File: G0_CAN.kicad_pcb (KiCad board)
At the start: 2 copper layers, 69.8 x 53.3 mm, 31 parts, among them J1 USB_C_Receptacle_USB2.0, J2 CAN1, J3 CAN2, U1 Nucleo-64-G0B1, U2 TJA1051TK-3, U3 TJA1051TK-3

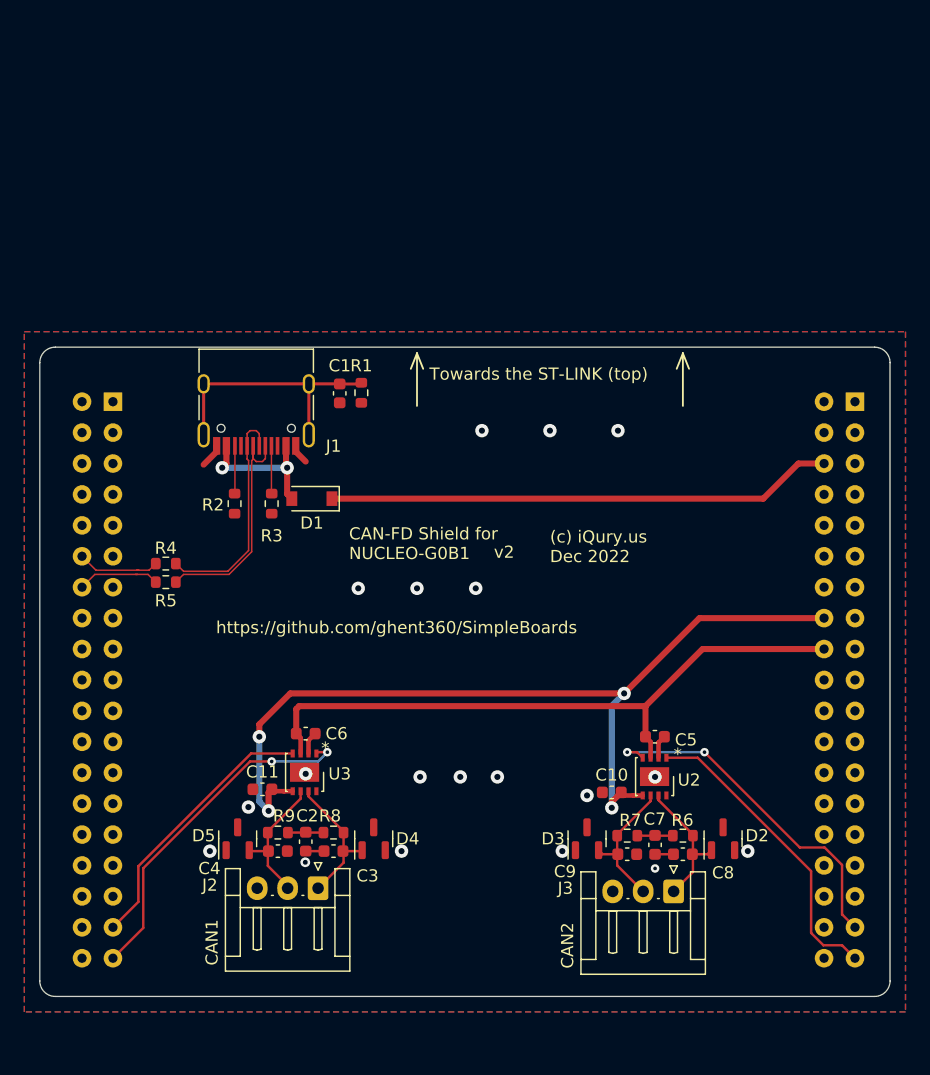
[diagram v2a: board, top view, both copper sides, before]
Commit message: Make the G0-CAN board use isolated CAN.
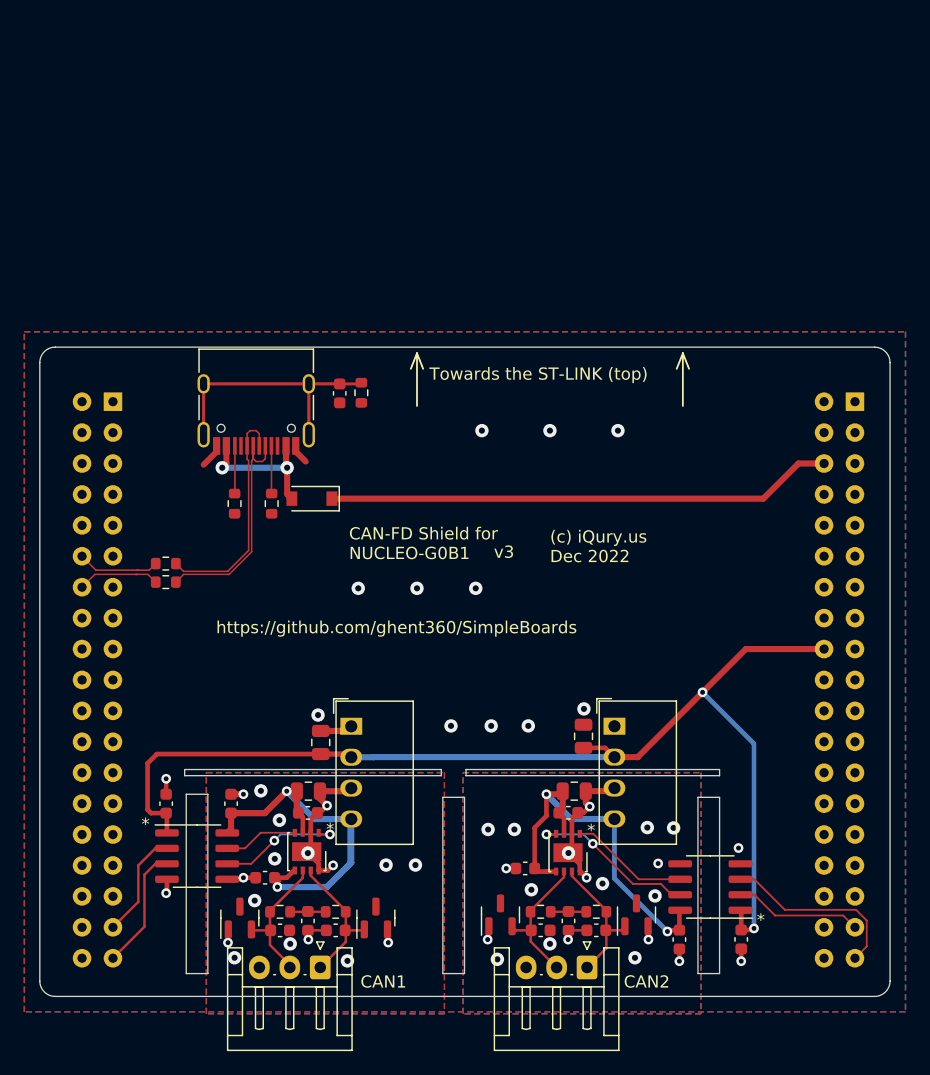
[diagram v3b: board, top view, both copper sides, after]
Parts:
- added C12: 4.7uF, Capacitor_SMD:C_0805_2012Metric, F.Cu at (96.0, 100.0)
- added C13: 4.7uF, Capacitor_SMD:C_0805_2012Metric, F.Cu at (96.7, 95.5)
- added C14: 4.7uF, Capacitor_SMD:C_0805_2012Metric, F.Cu at (74.1, 100.0)
- added C15: 4.7uF, Capacitor_SMD:C_0805_2012Metric, F.Cu at (75.1, 96.0)
- added C16: 100nF, Capacitor_SMD:C_0603_1608Metric, F.Cu at (62.4, 101.0)
- added C17: 100nF, Capacitor_SMD:C_0603_1608Metric, F.Cu at (67.8, 101.0)
- added C18: 100nF, Capacitor_SMD:C_0603_1608Metric, F.Cu at (109.7, 112.2)
- added C19: 100nF, Capacitor_SMD:C_0603_1608Metric, F.Cu at (104.6, 112.2)
- added U4: CRE1S0505S3C, Converter_DCDC:Converter_DCDC_Murata_CRE1xxxxxx3C_THT, F.Cu at (99.3, 94.6)
- added U5: CRE1S0505S3C, Converter_DCDC:Converter_DCDC_Murata_CRE1xxxxxx3C_THT, F.Cu at (77.7, 94.6)
- added U6: ADuM1201BR, Package_SO:SOIC-8_3.9x4.9mm_P1.27mm, F.Cu at (65.0, 105.3)
- added U7: ADuM1201BR, Package_SO:SOIC-8_3.9x4.9mm_P1.27mm, F.Cu at (107.2, 107.8)
- moved C10 9.47 mm to (91.9, 106.3)
- moved D3 9.47 mm to (89.9, 110.1)
- moved U2 9.47 mm to (95.5, 105.0)
- moved C5 9.47 mm to (95.5, 101.8)
- moved C7 9.47 mm to (95.5, 110.6)
- moved C8 9.47 mm to (97.8, 111.4)
- moved C9 9.47 mm to (93.2, 111.4)
- moved D2 9.47 mm to (101.1, 110.1)
- moved J3 9.47 mm to (97.0, 114.5)
- moved R6 9.47 mm to (97.8, 109.9)
- moved R7 9.47 mm to (93.2, 109.9)
- moved C11 7.27 mm to (70.6, 107.1)
- moved C3 6.51 mm to (76.4, 111.4)
- moved C4 6.51 mm to (71.8, 111.4)
- moved C6 6.51 mm to (74.1, 101.8)
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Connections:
- C10 pad 1: GND -> GND2
- C10 pad 2: /3.3V -> /5V-CAN2
- C11 pad 1: GND -> GND1
- C11 pad 2: /3.3V -> /5V-CAN1
- C2 pad 2: GND -> GND1
- C3 pad 2: GND -> GND1
- C4 pad 1: GND -> GND1
- C5 pad 1: /5V -> /5V-CAN2
- C5 pad 2: GND -> GND2
- C6 pad 1: /5V -> /5V-CAN1
- C6 pad 2: GND -> GND1
- C7 pad 2: GND -> GND2
- C8 pad 2: GND -> GND2
- C9 pad 1: GND -> GND2
- D2 pad 2: GND -> GND2
- D3 pad 1: GND -> GND2
- D4 pad 2: GND -> GND1
- D5 pad 1: GND -> GND1
- J2 pad 3: GND -> GND1
- J3 pad 3: GND -> GND2
- U2 pad 1: /CAN2_TX -> /CAN2_TX_ISO
- U2 pad 2: GND -> GND2
- U2 pad 3: /5V -> /5V-CAN2
- U2 pad 4: /CAN2_RX -> /CAN2_RX_ISO
- U2 pad 5: /3.3V -> /5V-CAN2
- U2 pad 8: GND -> GND2
- U2 pad 9: GND -> GND2
- U3 pad 1: /CAN1_TX -> /CAN1_TX_ISO
- U3 pad 2: GND -> GND1
- U3 pad 3: /5V -> /5V-CAN1
- U3 pad 4: /CAN1_RX -> /CAN1_RX_ISO
- U3 pad 5: /3.3V -> /5V-CAN1
- U3 pad 8: GND -> GND1
- U3 pad 9: GND -> GND1
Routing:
- net /3.3V: track 74.4 -> 0.00 mm, vias 4 -> 0
- net /5V: track 53.6 -> 96.2 mm, vias 0 -> 2
- net /5V-CAN1: track 0.00 -> 34.8 mm, vias 0 -> 2
- net /5V-CAN2: track 0.00 -> 33.8 mm, vias 0 -> 2
- net /CAN1_TX: track 28.4 -> 10.2 mm, vias 2 -> 0
- net /CAN2_RX: track 28.5 -> 10.5 mm, vias 2 -> 0
- net GND1: track 0.00 -> 17.0 mm, vias 0 -> 17
- net /CAN2_RX_ISO: track 0.00 -> 13.9 mm, vias 0 -> 2
- net GND2: track 0.00 -> 13.9 mm, vias 0 -> 19
- net /CAN1_RX: track 22.4 -> 8.88 mm
- net /CAN1_TX_ISO: track 0.00 -> 10.4 mm, vias 0 -> 2
- net /CAN2_TX: track 25.3 -> 15.3 mm
- net /CAN2_TX_ISO: track 0.00 -> 9.79 mm
- net /CAN1_RX_ISO: track 0.00 -> 6.09 mm
- net GND: track 10.4 -> 9.73 mm, vias 19 -> 15
- added copper zone on B.Cu, net GND1
- added copper zone on F.Cu, net GND1
- added copper zone on B.Cu, net GND2
- added copper zone on F.Cu, net GND2
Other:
- outline, holes or cut-outs redrawn
- board text added: "v3"
- board text removed: "v2"

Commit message: Flip the nucleo connector.
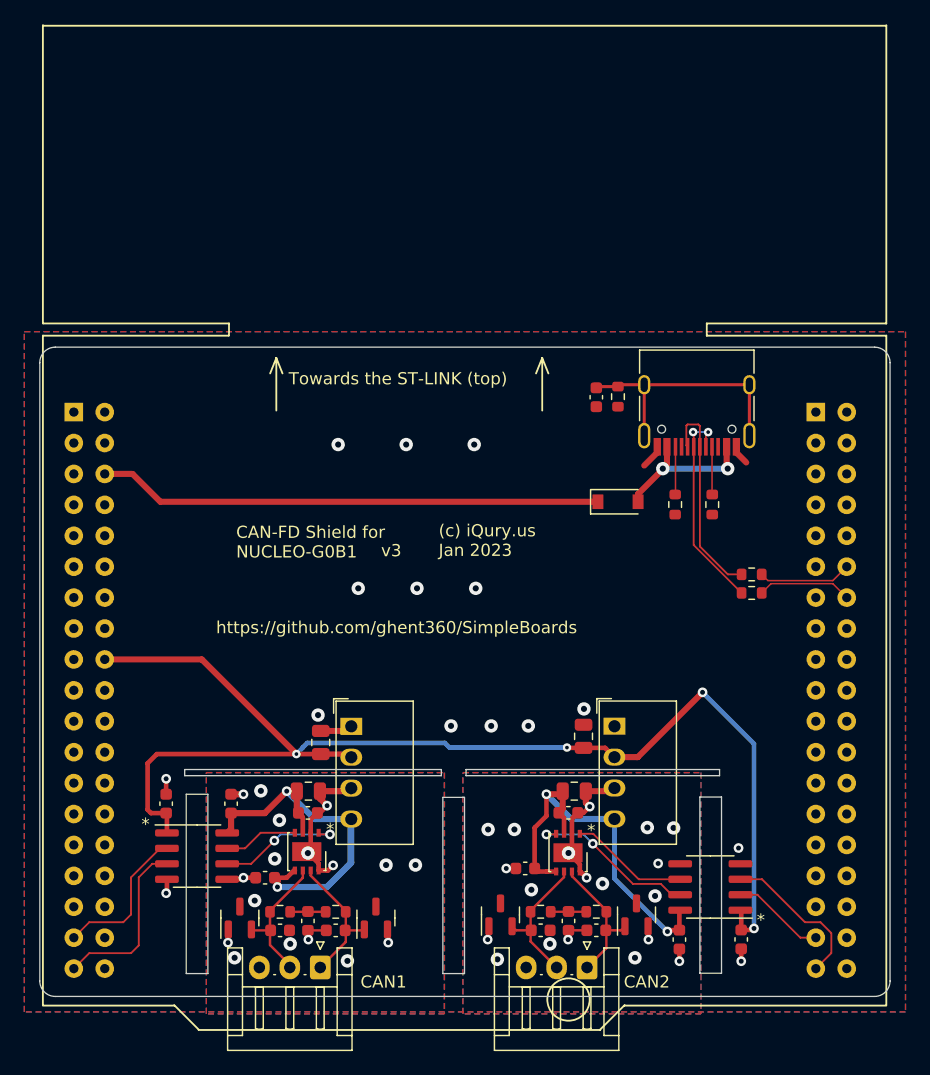
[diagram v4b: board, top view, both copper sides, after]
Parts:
- U1: moved to F.Cu
- U6, U7: value ADuM1201BR -> NSi8121N0
- moved U1 64.2 mm to (54.9, 114.6), turned to 0 degrees
- moved R4 48.1 mm to (110.6, 82.2), turned to 0 degrees
- moved R5 48.1 mm to (110.6, 83.7), turned to 0 degrees
- moved J1 36.2 mm to (106.0, 67.6)
- moved R2 36.2 mm to (104.3, 76.4)
- moved R3 36.2 mm to (107.3, 76.4)
- moved D1 25.1 mm to (99.6, 76.2), turned to 0 degrees
- moved C1 21.1 mm to (97.8, 67.6)
- moved R1 21.1 mm to (99.6, 67.6)
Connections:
- U1 pad 35: /CAN2_RX -> /CAN1_RX
- U1 pad 37: /CAN2_TX -> /CAN1_TX
- U1 pad 73: /CAN1_RX -> /CAN2_RX
- U1 pad 75: /CAN1_TX -> /CAN2_TX
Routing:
- net /5V: track 96.2 -> 106.3 mm, vias 2 -> 4
- net /CAN1_TX: track 10.2 -> 14.5 mm
- net /CAN1_RX: track 8.88 -> 12.5 mm
- net /CAN2_RX: track 10.5 -> 7.66 mm
- net /CAN2_TX: track 15.3 -> 12.7 mm
- net /D-: track 19.3 -> 17.4 mm, vias 0 -> 2
- net /D+: track 18.8 -> 17.3 mm
- net Net-(D1-A): track 11.8 -> 12.7 mm
- net /USB_DN: track 6.92 -> 7.78 mm
- net /USB_DP: track 6.92 -> 7.67 mm
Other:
- outline, holes or cut-outs redrawn
- board text added: "(c) iQury.us Jan 2023"
- board text removed: "(c) iQury.us Dec 2022"

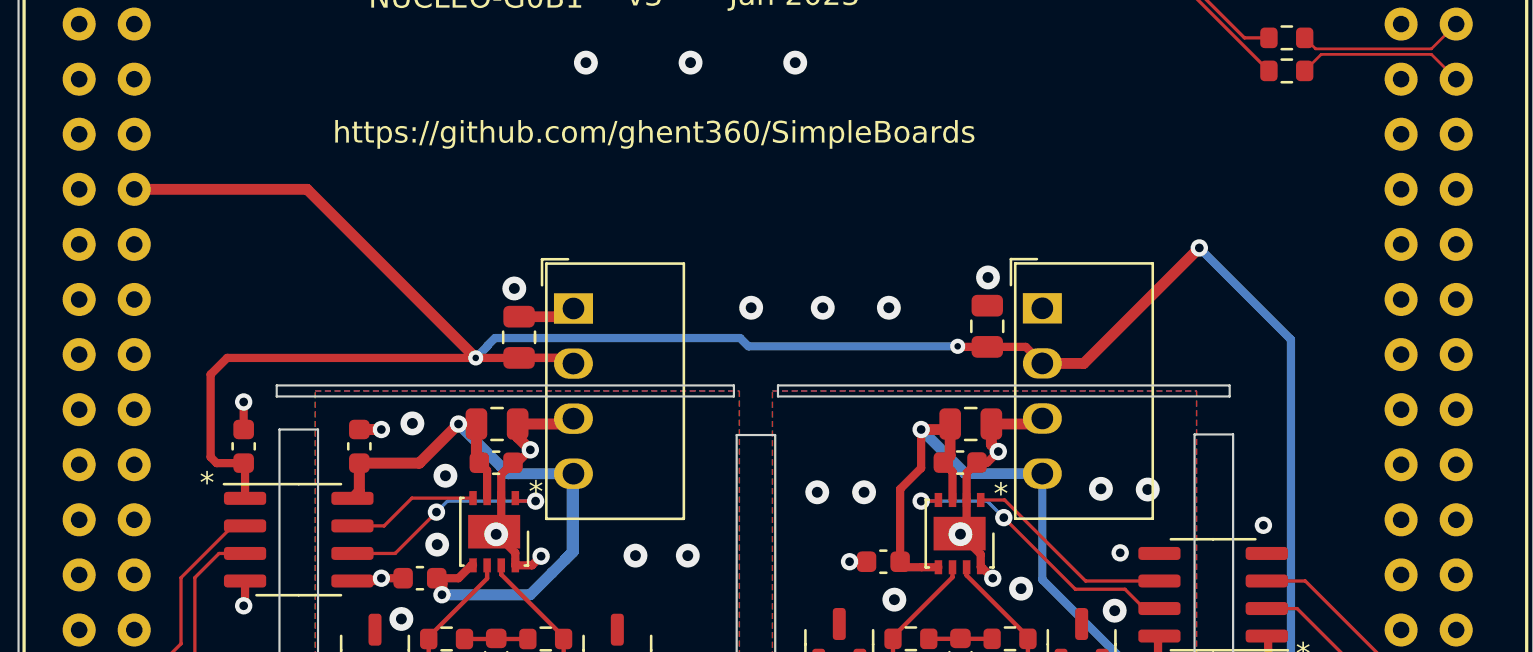
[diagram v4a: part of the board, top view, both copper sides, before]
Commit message: Add TX/RX leds to the CAN shield.
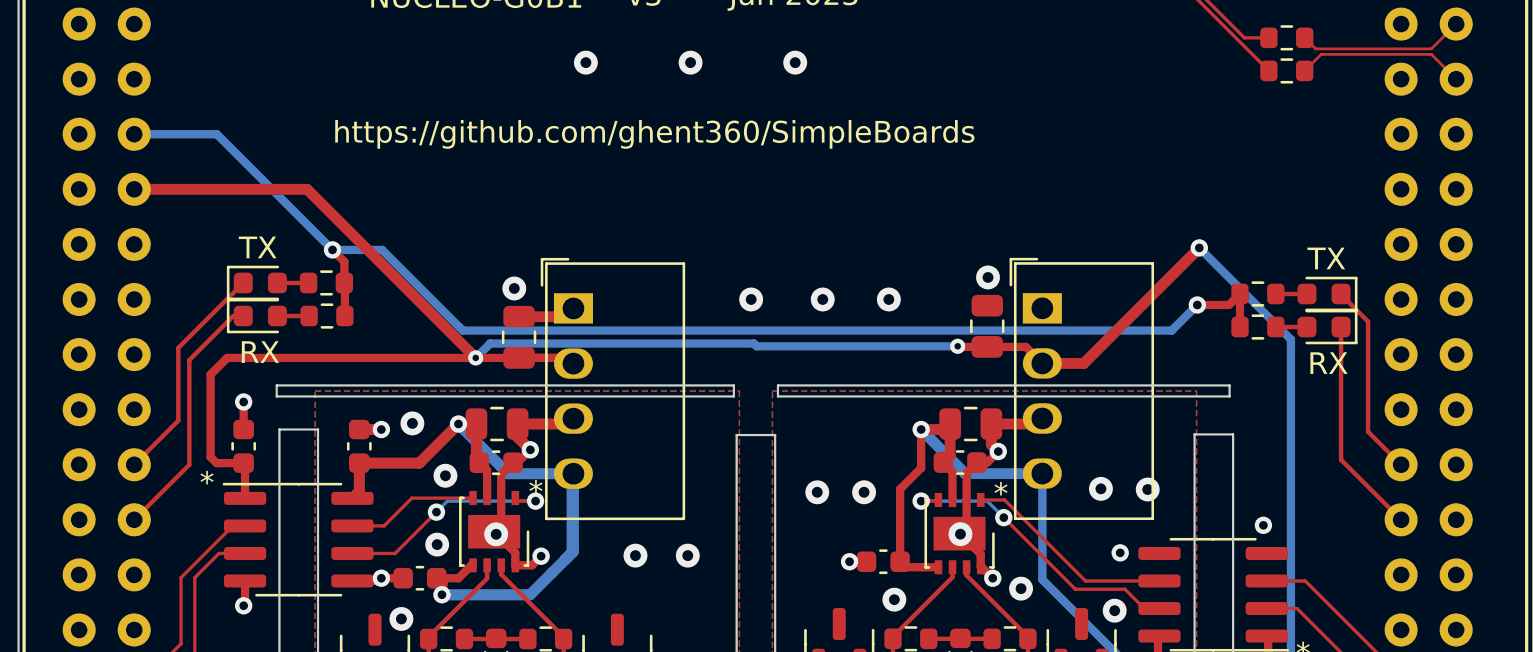
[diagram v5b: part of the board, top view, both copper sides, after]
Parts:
- added D6: TX, LED_SMD:LED_0603_1608Metric, F.Cu at (63.2, 93.5)
- added D7: TX, LED_SMD:LED_0603_1608Metric, F.Cu at (112.3, 94.0)
- added D8: RX, LED_SMD:LED_0603_1608Metric, F.Cu at (63.2, 95.0)
- added D9: RX, LED_SMD:LED_0603_1608Metric, F.Cu at (112.3, 95.5)
- added R10: 22, Resistor_SMD:R_0603_1608Metric, F.Cu at (66.3, 93.5)
- added R11: 22, Resistor_SMD:R_0603_1608Metric, F.Cu at (109.2, 94.0)
- added R12: 22, Resistor_SMD:R_0603_1608Metric, F.Cu at (66.3, 95.0)
- added R13: 22, Resistor_SMD:R_0603_1608Metric, F.Cu at (109.2, 95.5)
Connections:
- U1 pad 28: unconnected-(U1A-PA0) -> /CAN1_TX_LED
- U1 pad 30: unconnected-(U1A-PA1) -> /CAN1_RX_LED
- U1 pad 65: unconnected-(U1B-PB4) -> /CAN2_TX_LED
- U1 pad 67: unconnected-(U1B-PB5) -> /CAN2_RX_LED
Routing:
- net /3.3V: track 0.00 -> 60.2 mm, vias 0 -> 2
- net /CAN1_RX_LED: track 0.00 -> 11.7 mm
- net /CAN1_TX_LED: track 0.00 -> 10.5 mm
- net /CAN2_RX_LED: track 0.00 -> 10.0 mm
- net /CAN2_TX_LED: track 0.00 -> 9.02 mm
- net Net-(D8-A): track 0.00 -> 1.46 mm
- net Net-(D9-A): track 0.00 -> 1.44 mm
- net Net-(D7-A): track 0.00 -> 1.44 mm
- net Net-(D6-A): track 0.00 -> 1.44 mm
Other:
- board text added: "RX"
- board text added: "TX"

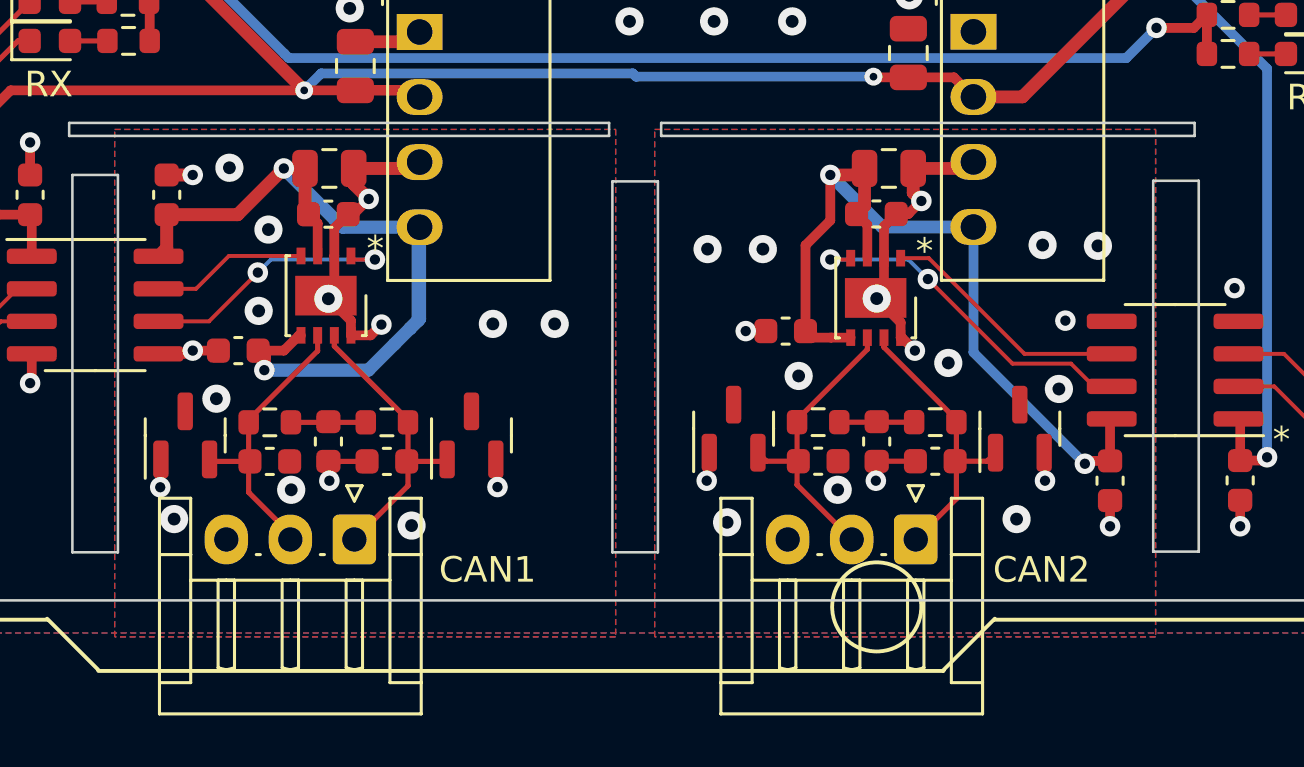
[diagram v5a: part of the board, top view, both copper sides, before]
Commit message: Add terminator jumpers.
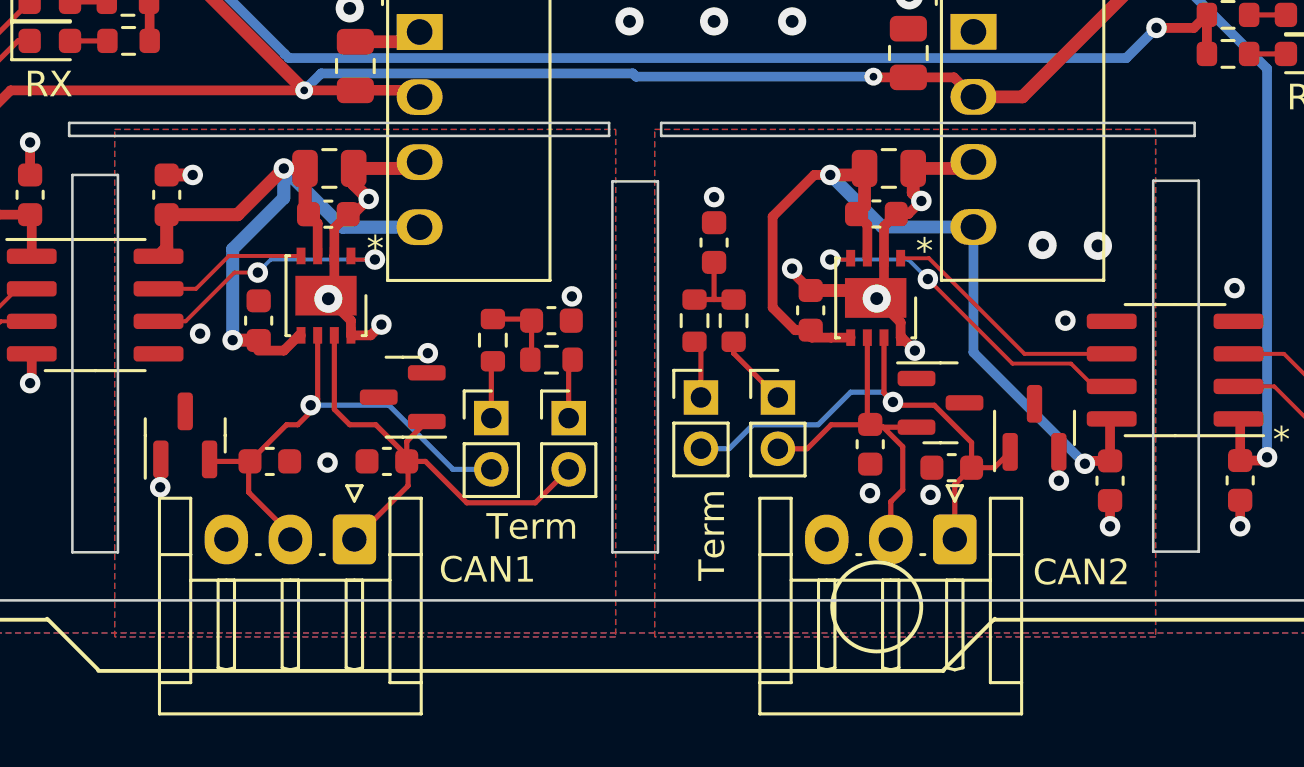
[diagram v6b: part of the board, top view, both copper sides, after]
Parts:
- added JP1: Trm, Connector_PinHeader_2.00mm:PinHeader_1x02_P2.00mm_Vertical, F.Cu at (88.6, 108.9)
- added JP2: Trm, Connector_PinHeader_2.00mm:PinHeader_1x02_P2.00mm_Vertical, F.Cu at (91.6, 108.9)
- added JP3: Trm, Connector_PinHeader_2.00mm:PinHeader_1x02_P2.00mm_Vertical, F.Cu at (83.5, 109.7)
- added JP4: Trm, Connector_PinHeader_2.00mm:PinHeader_1x02_P2.00mm_Vertical, F.Cu at (80.5, 109.7)
- moved R6 10.2 mm to (88.4, 105.9), turned to 90 degrees
- moved C7 10.0 mm to (89.2, 102.9), turned to 90 degrees
- moved C2 9.90 mm to (82.8, 105.9), turned to 0 degrees
- moved R9 9.28 mm to (80.5, 106.7), turned to 90 degrees
- moved D3 8.14 mm to (98.0, 109.1), turned to 0 degrees
- moved R8 6.87 mm to (82.8, 107.4)
- moved R7 5.16 mm to (89.9, 105.9), turned to 90 degrees
- moved D4 3.07 mm to (77.0, 108.9), turned to 180 degrees
- moved C9 2.14 mm to (95.2, 110.7), turned to 90 degrees
- moved J3 1.52 mm to (98.6, 114.5)
- moved C11 1.42 mm to (71.4, 105.9), turned to -90 degrees
- moved C10 1.27 mm to (92.9, 105.5), turned to -90 degrees
- moved C8 0.69 mm to (98.4, 111.7)
- moved D2 0.57 mm to (101.7, 110.1)
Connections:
- R6 pad 1: /CAN2_H -> Net-(JP1-A)
- R7 pad 1: Net-(C7-Pad1) -> Net-(JP2-A)
- R7 pad 2: /CAN2_L -> Net-(C7-Pad1)
- R8 pad 1: /CAN1_H -> Net-(JP3-A)
- R9 pad 1: Net-(C2-Pad1) -> Net-(JP4-A)
- R9 pad 2: /CAN1_L -> Net-(C2-Pad1)
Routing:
- net /CAN2_H: track 11.4 -> 20.8 mm, vias 0 -> 1
- net /CAN1_L: track 11.4 -> 20.1 mm, vias 0 -> 1
- net /CAN1_H: track 11.6 -> 20.0 mm
- net /5V-CAN1: track 34.8 -> 28.3 mm
- net GND1: track 17.0 -> 13.1 mm, vias 17 -> 9
- net Net-(JP2-A): track 0.00 -> 2.89 mm
- net /CAN2_L: track 11.6 -> 14.2 mm
- net Net-(JP3-A): track 0.00 -> 2.35 mm
- net GND2: track 13.9 -> 16.2 mm, vias 19 -> 12
- net Net-(JP1-A): track 0.00 -> 2.28 mm
- net Net-(JP4-A): track 0.00 -> 2.24 mm
- net /5V-CAN2: track 33.8 -> 35.6 mm
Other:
- board text added: "Term"
